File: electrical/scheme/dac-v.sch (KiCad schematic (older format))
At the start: 14 parts

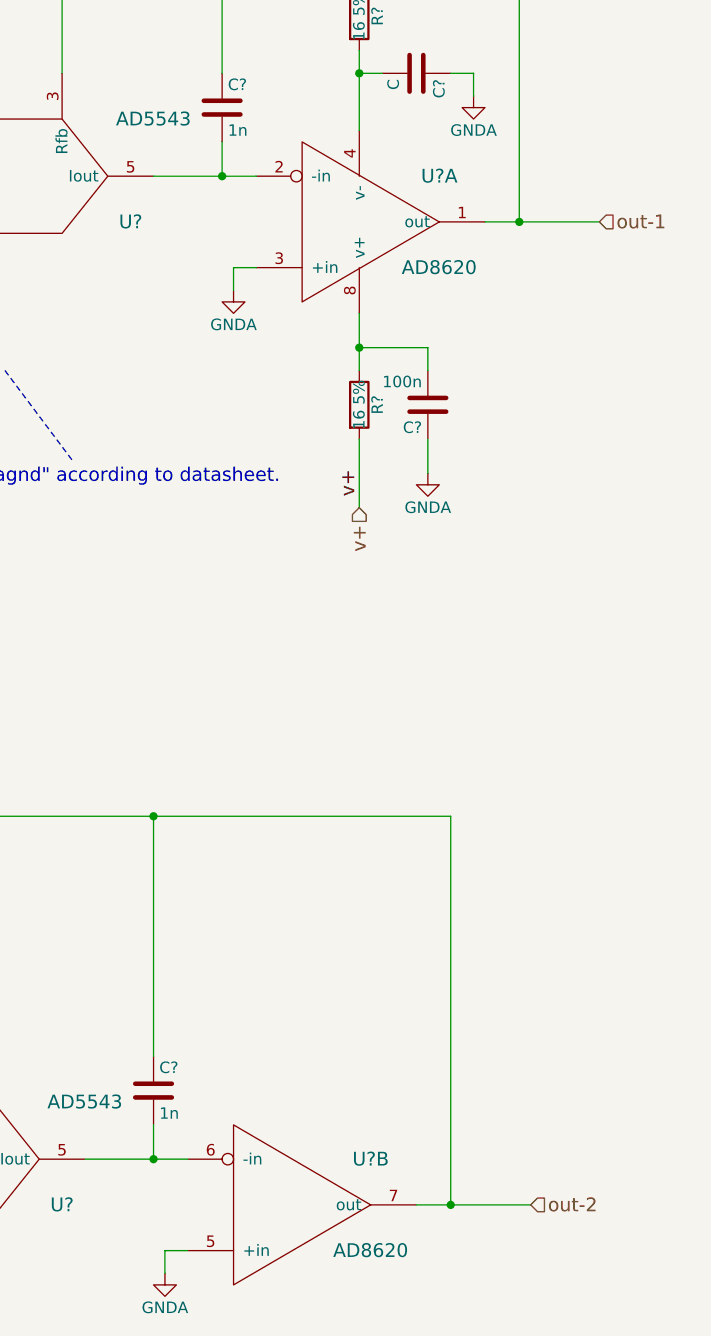
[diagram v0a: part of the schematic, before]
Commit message: Annotated opamps.
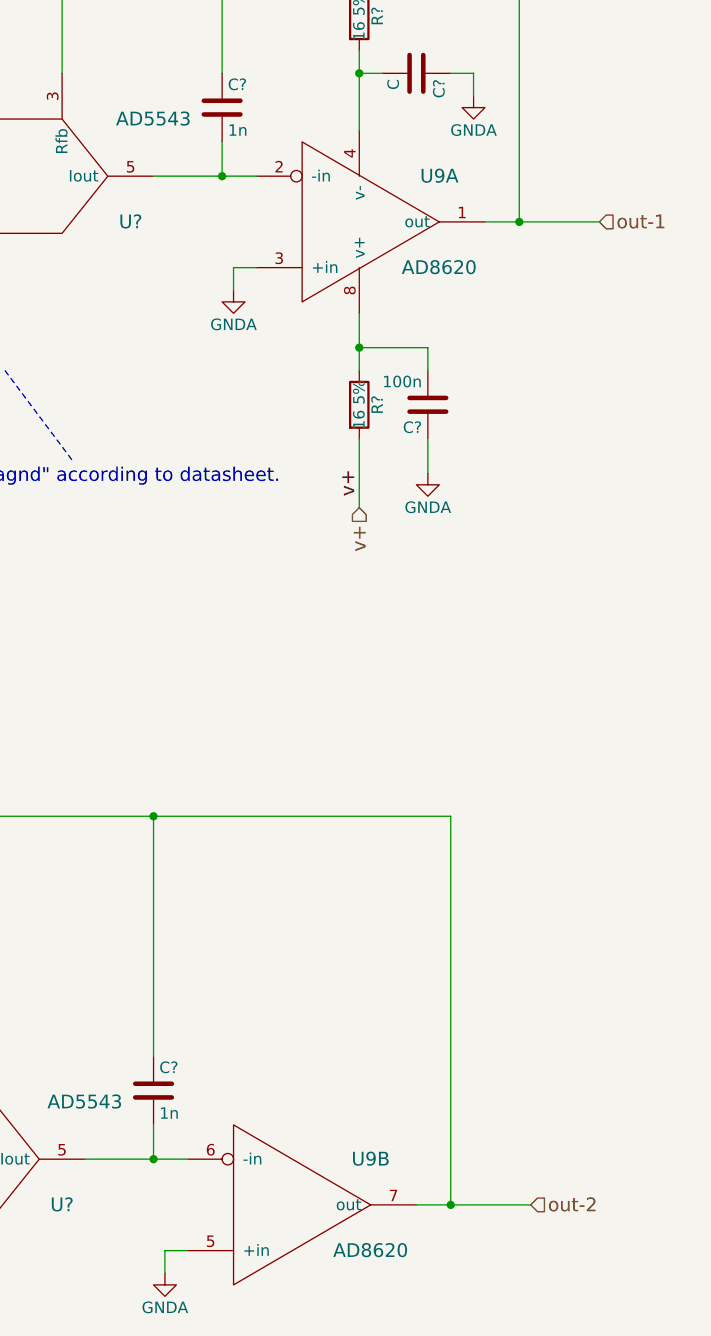
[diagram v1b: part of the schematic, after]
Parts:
- gave numbers to parts that had none: 1
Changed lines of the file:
@@
 	7800 6000 7800 7650
 $Comp
-L AD8620 U?
+L AD8620 U8
 U 2 1 55A0AE3F
 P 9400 8300
-AR Path="/55A0A529/55A0AE3F" Ref="U?"  Part="2"
-AR Path="/55A5B809/55A0AE3F" Ref="U?"  Part="2"
-F 0 "U?" H 9750 8100 60  0000 C CNN
+AR Path="/55A0A529/55A0AE3F" Ref="U8"  Part="2"
+AR Path="/55A5B809/55A0AE3F" Ref="U9"  Part="2"
+F 0 "U9" H 9750 8100 60  0000 C CNN
 F 1 "AD8620" H 9750 8500 60  0000 C CNN
 F 2 "" H 9450 8300 60  0000 C CNN
@@
 	8100 1700 8100 3350
 $Comp
-L AD8620 U?
+L AD8620 U8
 U 1 1 55A0B796
 P 9700 4000
-AR Path="/55A0A529/55A0B796" Ref="U?"  Part="1"
-AR Path="/55A5B809/55A0B796" Ref="U?"  Part="1"
-F 0 "U?" H 10050 3800 60  0000 C CNN
+AR Path="/55A0A529/55A0B796" Ref="U8"  Part="1"
+AR Path="/55A5B809/55A0B796" Ref="U9"  Part="1"
+F 0 "U9" H 10050 3800 60  0000 C CNN
 F 1 "AD8620" H 10050 4200 60  0000 C CNN
 F 2 "" H 9750 4000 60  0000 C CNN

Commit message: a
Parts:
- C64, C65, C66, C67, C68, C69, C71: renamed from C?; footprint (none) -> Capacitors_SMD:C_0805_HandSoldering
- C70: renamed from C?; value C -> 100n; footprint (none) -> Capacitors_SMD:C_0805_HandSoldering
- R67, R68: renamed from R?; footprint (none) -> Resistors_SMD:R_0805_HandSoldering
- U21, U22: renamed from U?; footprint (none) -> Housings_SOIC:SOIC-8_3.9x4.9mm_Pitch1.27mm
- U8: value AD8620 -> AD8672; footprint (none) -> Housings_SOIC:SOIC-8_3.9x4.9mm_Pitch1.27mm
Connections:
- wire segments 52 -> 54
